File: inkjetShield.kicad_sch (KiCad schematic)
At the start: 0 parts

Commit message: skeletan schematic established
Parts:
- added U1: Teensy4.1, teensy:Teensy41, symbol teensy:Teensy4.1
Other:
- note added: "HIGH VOLTAGE BOOST CONVERTER"
- note added: "LEDS & SWITCHES"
- note added: "MCU (Teensy 4.1)"
- note added: "OLED + OLED DRIVER"
- note added: "SHIFT REGISTER DRIVER"
- note added: "adjustable boost converter, up to 90V (max)"
- note added: "hv507"
- note added: "several switches and leds for general purpose diagnostics"
- note added: "this is optional, unsure if we need it"

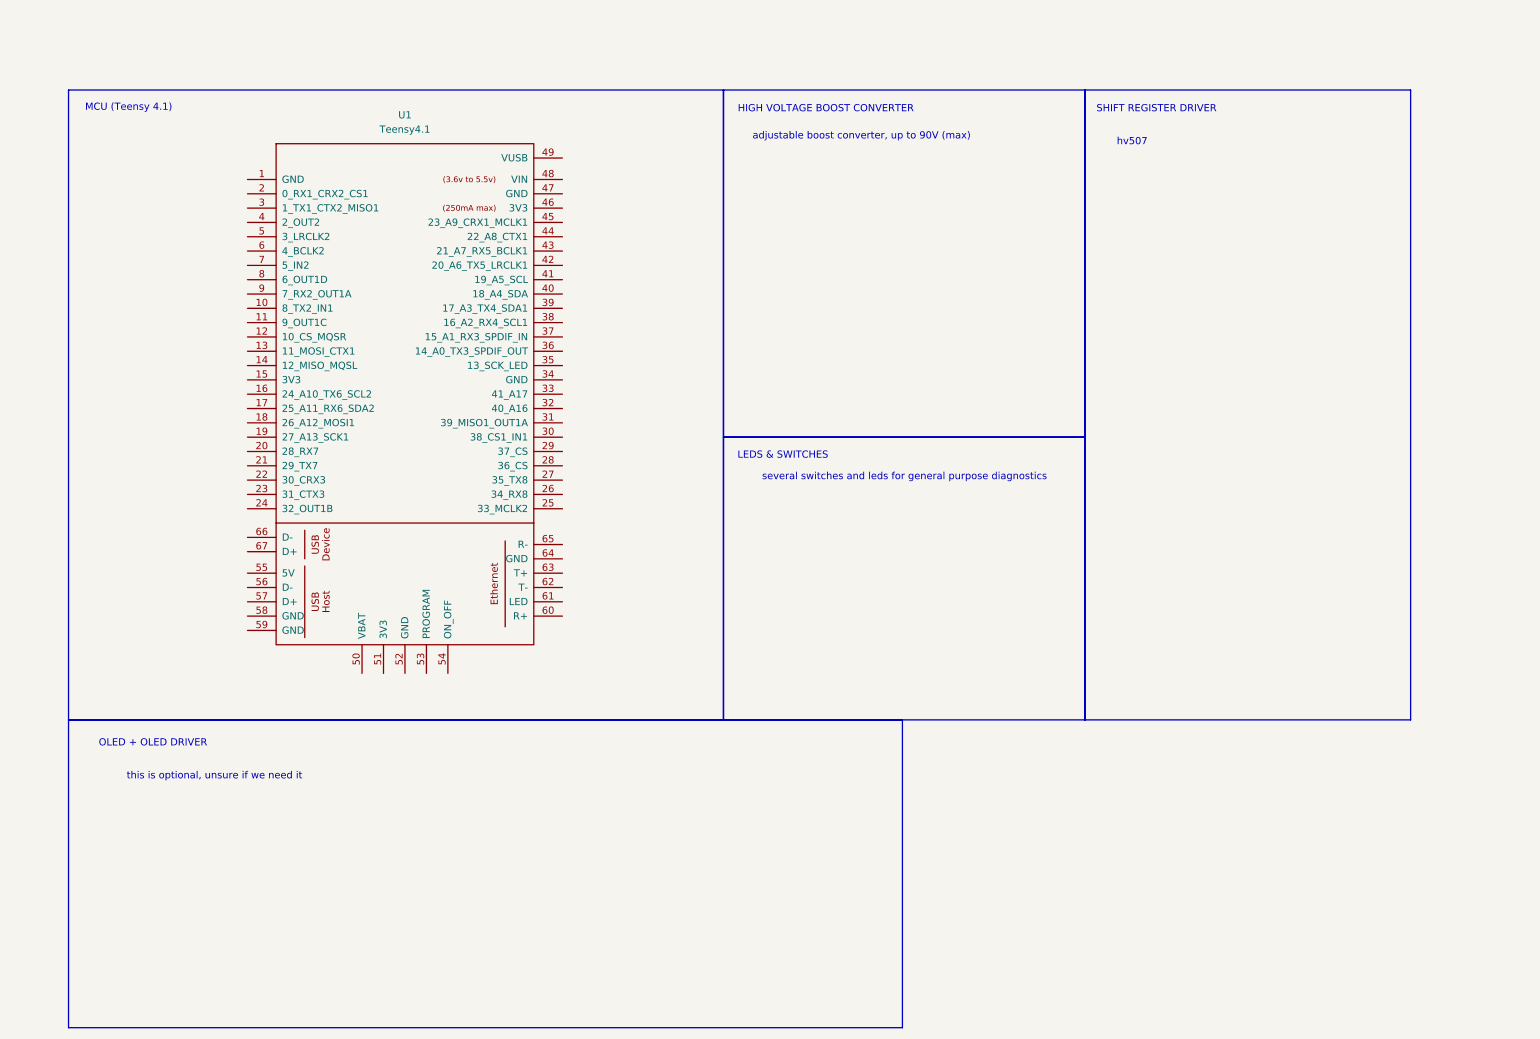
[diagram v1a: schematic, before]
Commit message: identified target components and updated schematic
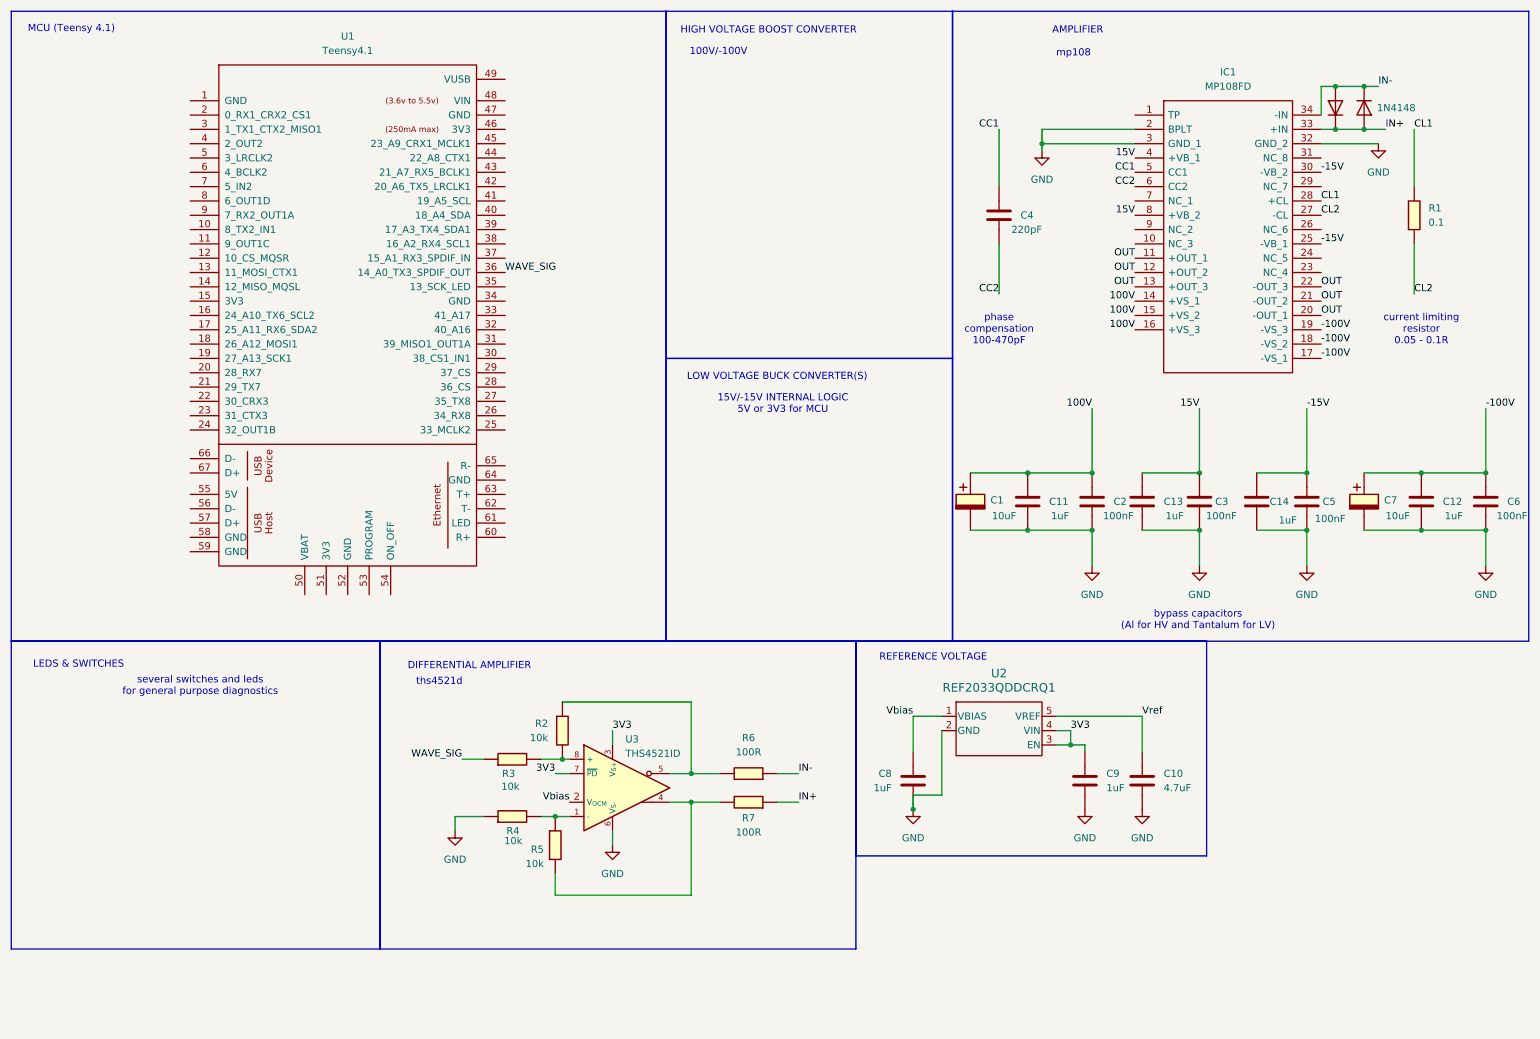
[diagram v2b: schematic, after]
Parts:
- added C1, C7: 10uF, fab:CP_Elec_D8.0mm_H16.0mm_TH_P3.5mm, symbol fab:CP_Elec_D8.0mm_H16.0mm_TH_P3.5mm
- added C10: 4.7uF, fab:C_1206, symbol fab:C_1206
- added C11, C12, C13, C14, C8, C9: 1uF, fab:C_1206, symbol fab:C_1206
- added C2, C3, C5, C6: 100nF, fab:C_1206, symbol fab:C_1206
- added C4: 220pF, fab:C_1206, symbol fab:C_1206
- added IC1: MP108FD, custom:MP108FD, symbol custom:MP108FD
- added R1: 0.1, fab:R_1206, symbol fab:R_1206
- added R2, R3, R4, R5: 10k, fab:R_1206, symbol fab:R_1206
- added R6, R7: 100R, fab:R_1206, symbol fab:R_1206
- added U2: REF2033QDDCRQ1, Snapeda:SOT-23-THIN-5_DDC_TEX, symbol SnapEDA3:REF2033QDDCRQ1
- added U3: THS4521ID, Package_SO:VSSOP-8_3x3mm_P0.65mm, symbol Amplifier_Difference:THS4521ID
- added Z1, Z2: 1N4148, fab:SOD-123, symbol Device:D
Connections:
- net WAVE_SIG: now reaches U1.36 (14_A0_TX3_SPDIF_OUT)
- net WAVE_SIG: now also R3.2
- new net: R2.1, R3.1, U3.8 (+)
- new net: R2.2, R6.1, U3.5
- new net: R4.1, R5.2, U3.1 (-)
- new net: R5.1, R7.1, U3.4
- new net -100V: C12.1, C6.1, C7.1, IC1.17 (-VS_1), IC1.18 (-VS_2), IC1.19 (-VS_3)
- new net -15V: C14.1, C5.1, IC1.25 (-VB_1), IC1.30 (-VB_2)
- new net 100V: C1.1, C11.1, C2.1, IC1.14 (+VS_1), IC1.15 (+VS_2), IC1.16 (+VS_3)
- new net 15V: C13.1, C3.1, IC1.4 (+VB_1), IC1.8 (+VB_2)
- new net 3V3: C9.1, U2.3 (EN), U2.4 (VIN), U3.3 (V_{S+}), U3.7 (~{PD})
- new net CC1: C4.1, IC1.5 (CC1)
- new net CC2: C4.2, IC1.6 (CC2)
- new net CL1: IC1.28 (+CL), R1.1
- new net CL2: IC1.27 (-CL), R1.2
- new net GND: C1.2, C10.2, C11.2, C12.2, C13.2, C14.2, C2.2, C3.2, C5.2, C6.2, C7.2, C8.2, C9.2, IC1.2 (BPLT), IC1.3 (GND_1), IC1.32 (GND_2), R4.2, U2.2 (GND), U3.6 (V_{S-})
- new net IN+: IC1.33 (+IN), R7.2, Z1.2 (A), Z2.1 (K)
- new net IN-: IC1.34 (-IN), R6.2, Z1.1 (K), Z2.2 (A)
- new net OUT: IC1.11 (+OUT_1), IC1.12 (+OUT_2), IC1.13 (+OUT_3), IC1.20 (-OUT_1), IC1.21 (-OUT_2), IC1.22 (-OUT_3)
- new net Vbias: C8.1, U2.1 (VBIAS), U3.2 (V_{OCM})
- new net Vref: C10.1, U2.5 (VREF)
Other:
- note added: "100V/-100V"
- note added: "15V/-15V INTERNAL LOGIC 5V or 3V3 for MCU"
- note added: "AMPLIFIER"
- note added: "DIFFERENTIAL AMPLIFIER"
- note added: "LOW VOLTAGE BUCK CONVERTER(S)"
- note added: "REFERENCE VOLTAGE"
- note added: "bypass capacitors (Al for HV and Tantalum for LV)"
- note added: "current limiting resistor 0.05 - 0.1R"
- note added: "mp108"
- note added: "phase compensation 100-470pF"
- note added: "ths4521d"
- note removed: "OLED + OLED DRIVER"
- note removed: "SHIFT REGISTER DRIVER"
- note removed: "adjustable boost converter, up to 90V (max)"
- note removed: "hv507"
- note removed: "this is optional, unsure if we need it"
- moved on the sheet: U1
